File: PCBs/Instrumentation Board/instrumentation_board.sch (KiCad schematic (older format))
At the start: 10 parts

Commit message: Instrumentation board for review
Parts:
- added C1: .47uF, symbol C
- added C2: .1uF, symbol C
- added C3, C4: 100nF, symbol C
- added C5: 1uF, symbol C
- added U1: TPS71518DCKR, symbol TPS71518DCKR
- added U2: LSM6DS3HTR, symbol LSM6DS3HTR
- added U3: S-5851AAA-M6T1U, symbol S-5851AAA-M6T1U
- gave numbers to parts that had none: 10
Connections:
- net labels added: IMU_SCL, IMU_SDA, INT0, INT1, TEMP_SCL, TEMP_SDA
- wire segments 27 -> 54

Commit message: Changes requested by alex
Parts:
- removed U3: S-5851AAA-M6T1U, symbol S-5851AAA-M6T1U
- added C9: 100nF, symbol C
- added U3: LSM6DS3HTR, symbol LSM6DS3HTR
- C5: value 1uF -> 100nF
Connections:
- net labels added: SCL, SDA
- net labels removed: ALTIMETER_SCL, ALTIMETER_SDA, ARDUINO_SCL, ARDUINO_SDA, IMU_SCL, IMU_SDA, TEMP_SCL, TEMP_SDA
- no-connect marks 0 -> 33
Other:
- note added: "1.8V"
- moved on the sheet: A1, C1, C2, C3, C4, C6, C7, C8, J1, J2, U1, U2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

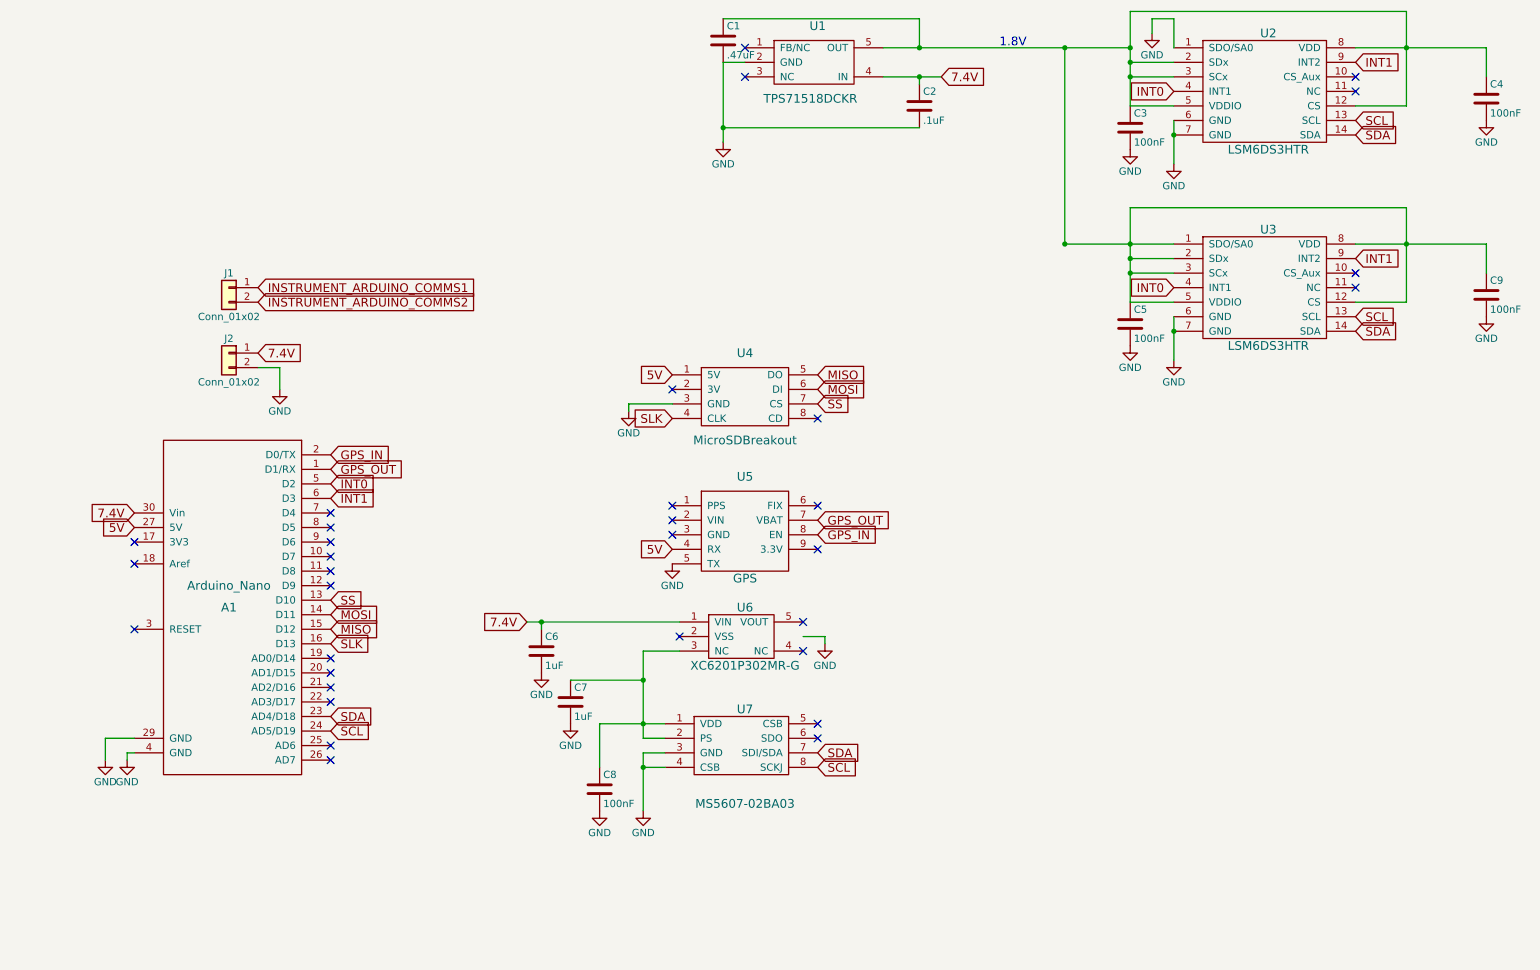
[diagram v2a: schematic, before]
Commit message: added some new parts and i2c bus changes
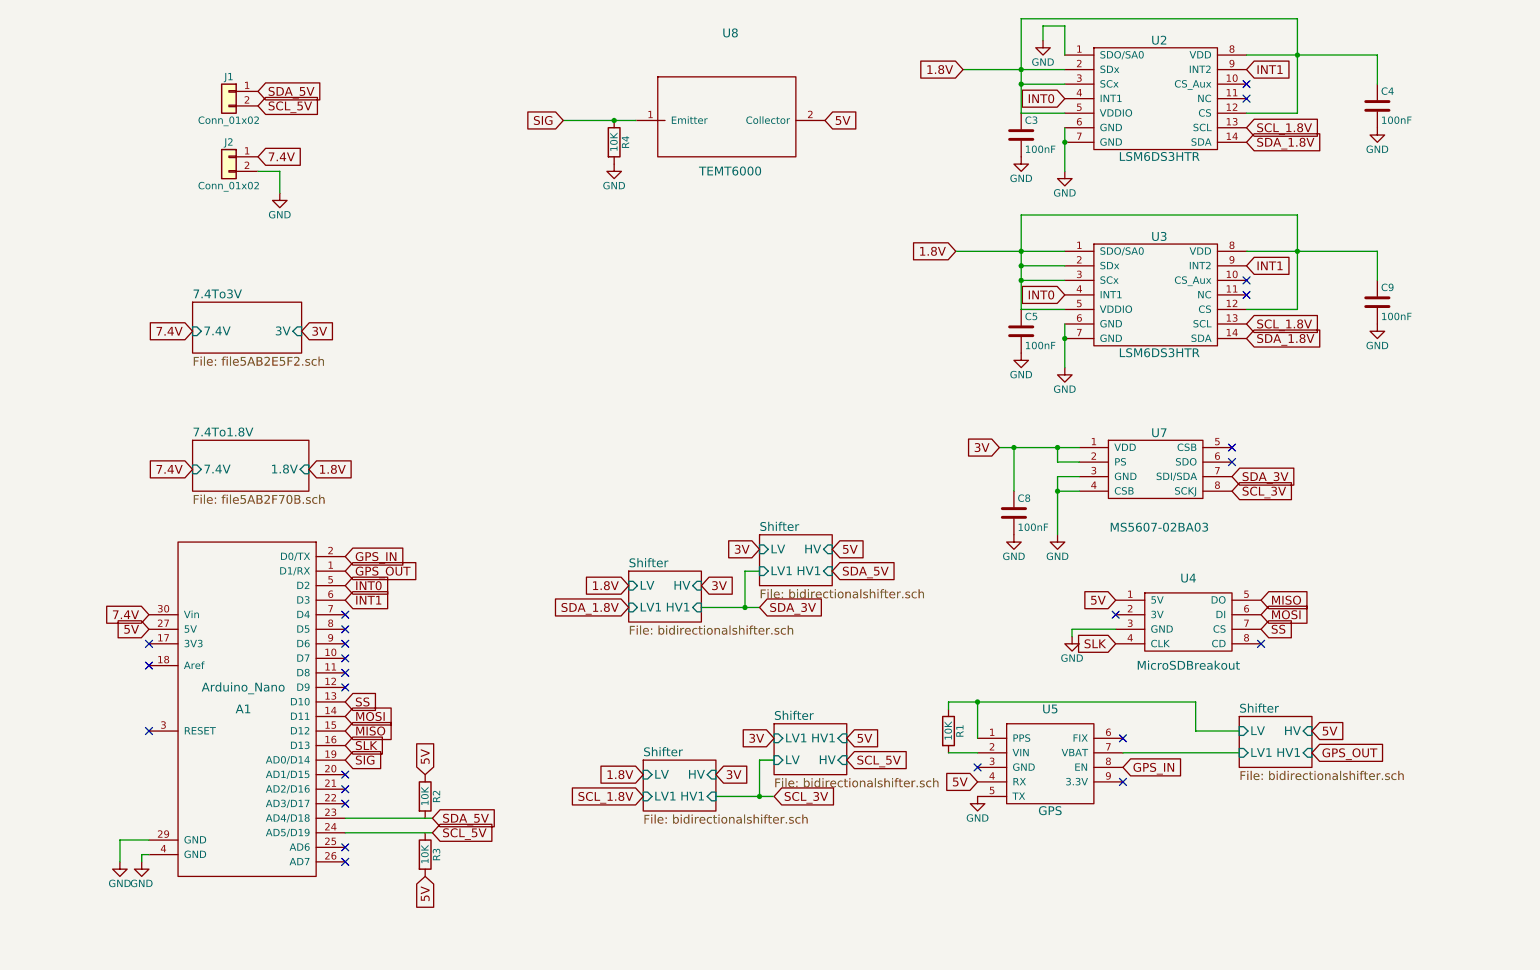
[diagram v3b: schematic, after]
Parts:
- removed C1: .47uF, symbol C
- removed C2: .1uF, symbol C
- removed C6, C7: 1uF, symbol C
- removed U1: TPS71518DCKR, symbol TPS71518DCKR
- removed U6: XC6201P302MR-G, symbol XC6201P302MR-G
- added R1, R2, R3, R4: 10K, symbol R
- added U8: TEMT6000, symbol TEMT6000
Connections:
- net 5V: now also R2.1, R3.2, U8.2 (Collector)
- net GND: now also R4.2
- net GPS_OUT: no longer U5.7 (VBAT)
- net SIG: now reaches A1.19 (AD0/D14)
- net SIG: now also R4.1, U8.1 (Emitter)
- net Shifter/LV: now reaches U5.1 (PPS)
- net Shifter/LV: now also R1.1
- net at U5.2 (VIN): now also R1.2
- net 3V: now reaches C8.1, U7.1 (VDD), U7.2 (PS)
- net 1.8V: now reaches C3.1, C4.1, C5.1, C9.1, U2.12 (CS), U2.2 (SDx), U2.3 (SCx), U2.5 (VDDIO), U2.8 (VDD), U3.1 (SDO/SA0), U3.12 (CS), U3.2 (SDx), U3.3 (SCx), U3.5 (VDDIO), U3.8 (VDD)
- net INSTRUMENT_ARDUINO_COMMS1 renamed SDA_5V
- net SDA_5V: now also A1.23 (AD4/D18)
- net INSTRUMENT_ARDUINO_COMMS2 renamed SCL_5V
- net SCL_5V: now also A1.24 (AD5/D19)
- net SCL renamed SCL_1.8V
- net SCL_1.8V: no longer A1.24 (AD5/D19), U7.8 (SCKJ)
- net SDA renamed SDA_1.8V
- net SDA_1.8V: no longer A1.23 (AD4/D18), U7.7 (SDI/SDA)
- new net SCL_3V: U7.8 (SCKJ)
- new net SDA_3V: U7.7 (SDI/SDA)
- new net Shifter/LV1: U5.7 (VBAT)
- no-connect marks 33 -> 25
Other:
- note removed: "1.8V"
- moved on the sheet: A1, C3, C4, C5, C8, C9, J1, J2, U2, U3, U4, U5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

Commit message: replace bidirectional shifters with ICs
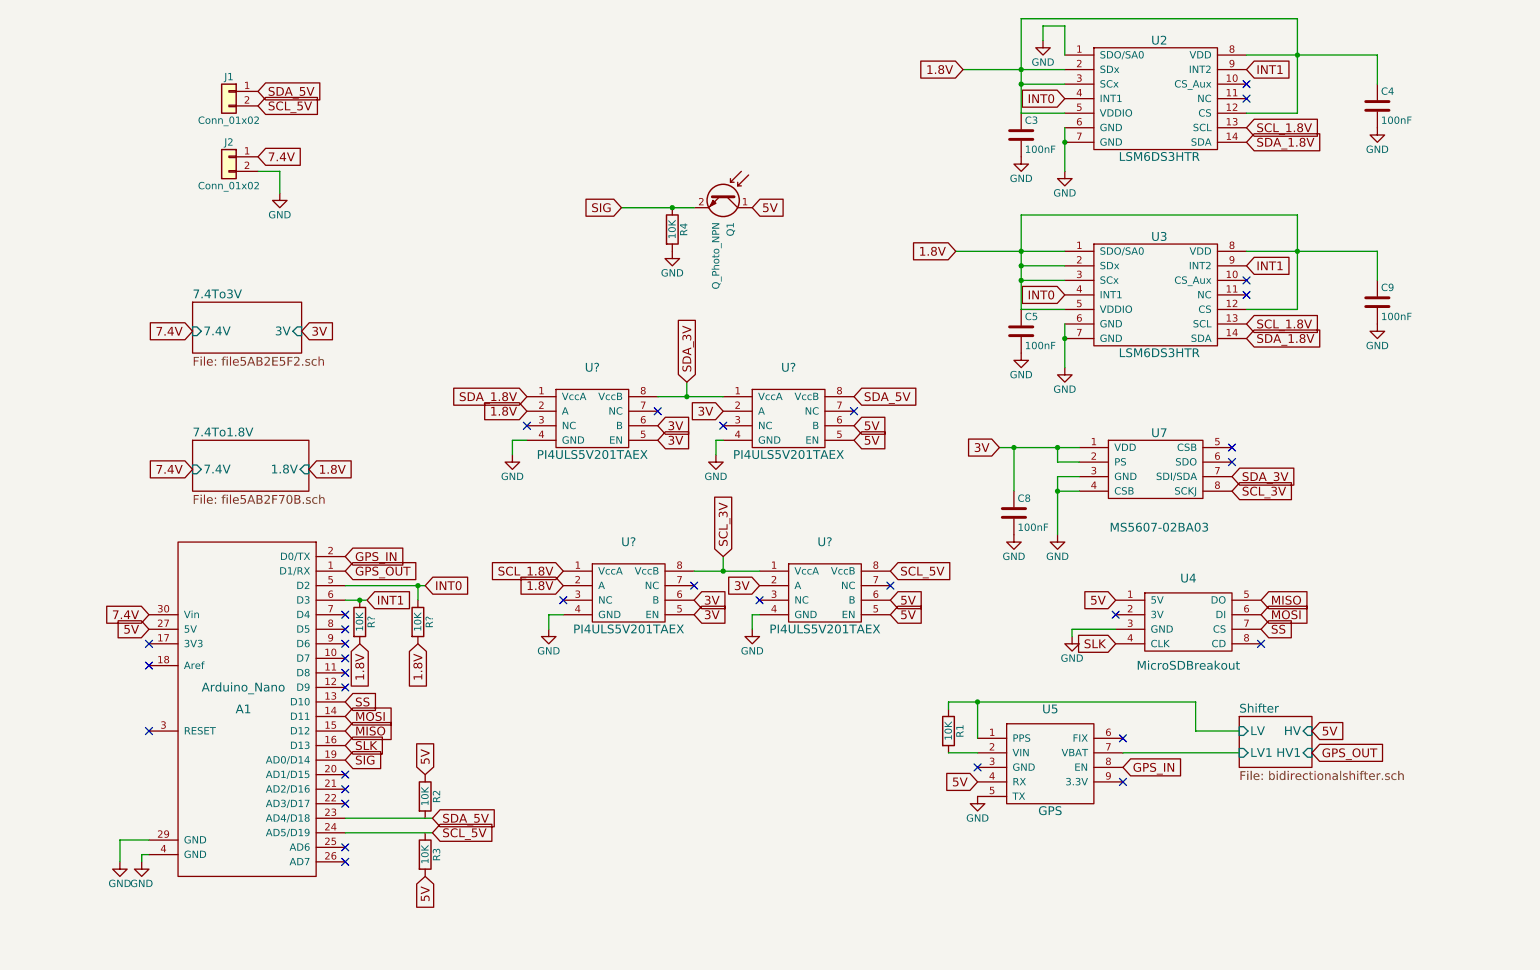
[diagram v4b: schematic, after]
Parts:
- removed U8: TEMT6000, symbol TEMT6000
- added Q1: Q_Photo_NPN, symbol Q_Photo_NPN
- added R? (x2): 10K, symbol R
- added U? (x4): PI4ULS5V201TAEX, symbol PI4ULS5V201TAEX
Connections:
- net 1.8V: now also R?.2, R?.2, U?.2 (A), U?.2 (A)
- net 3V: now also U?.2 (A), U?.2 (A), U?.5 (EN), U?.5 (EN), U?.6 (B), U?.6 (B)
- net 5V: now also Q1.1 (C), U?.5 (EN), U?.5 (EN), U?.6 (B), U?.6 (B)
- net GND: now also U?.4 (GND), U?.4 (GND), U?.4 (GND), U?.4 (GND)
- net INT0: now also R?.1
- net INT1: now also R?.1
- net SCL_1.8V: now also U?.1 (VccA)
- net SCL_3V: now also U?.1 (VccA), U?.8 (VccB)
- net SCL_5V: now also U?.8 (VccB)
- net SDA_1.8V: now also U?.1 (VccA)
- net SDA_3V: now also U?.1 (VccA), U?.8 (VccB)
- net SDA_5V: now also U?.8 (VccB)
- net SIG: now also Q1.2 (E)
- no-connect marks 25 -> 33
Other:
- moved on the sheet: R4
